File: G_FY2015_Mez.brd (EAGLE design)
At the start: 160 x 100 mm, 205 parts, among them IC100 FT232RL, IC101 FT245RL, J100 EPL.00.250.NTN, J101 IL-2P-S3EN2, J110 EPL.00.250.NTN, J111 IL-2P-S3EN2, J120 EPL.00.250.NTN, J121 IL-2P-S3EN2, J130 EPL.00.250.NTN, J131 IL-2P-S3EN2, J180 TOKUDEN_SP6, J181 USB Mini-B Connector, J182 USB Mini-B Connector, J300 SHV_PIGTAIL_LAND, J301 SHV_PIGTAIL_LAND, J400 RPI2_GPIO_HOLES, J410 IL-3P-S3EN2, J411 IL-3P-S3EN2, J600_12V IL-4P-S3EN2, J610 2.1MMJACKTHM, J620 IL-2P-S3EN2, J630 USB_TYPEA_LUMBERG_2410_01, J640 USB_TYPEA_LUMBERG_2410_01, J650_VOUT IL-4P-S3EN2, U100 AD9215LONG_PAD, U101 AD8138, U102 LM6172, U110 AD9215LONG_PAD, U111 AD8138, U112 LM6172, U120 AD9215LONG_PAD, U121 AD8138, U130 AD9215LONG_PAD, U131 AD8138, U191 GPS_FGPMMOPA6H, U300 OPTON_1PA_12, U301 OPTON_1PA_12, U302 2SC1815, U303 2SJ681, U410 MCP3208-CI/SL, U411 MCP1525TSOT-23-3, U412 LM60, U413 LM60, U500 LT6106, U510 LT6106, U520 2SC1815, U521 2SJ681, U600 PHT12050WAH, U610 PHT12050WAH, U620 LTC1983ES6-3, U621 LTC1983ES6-5

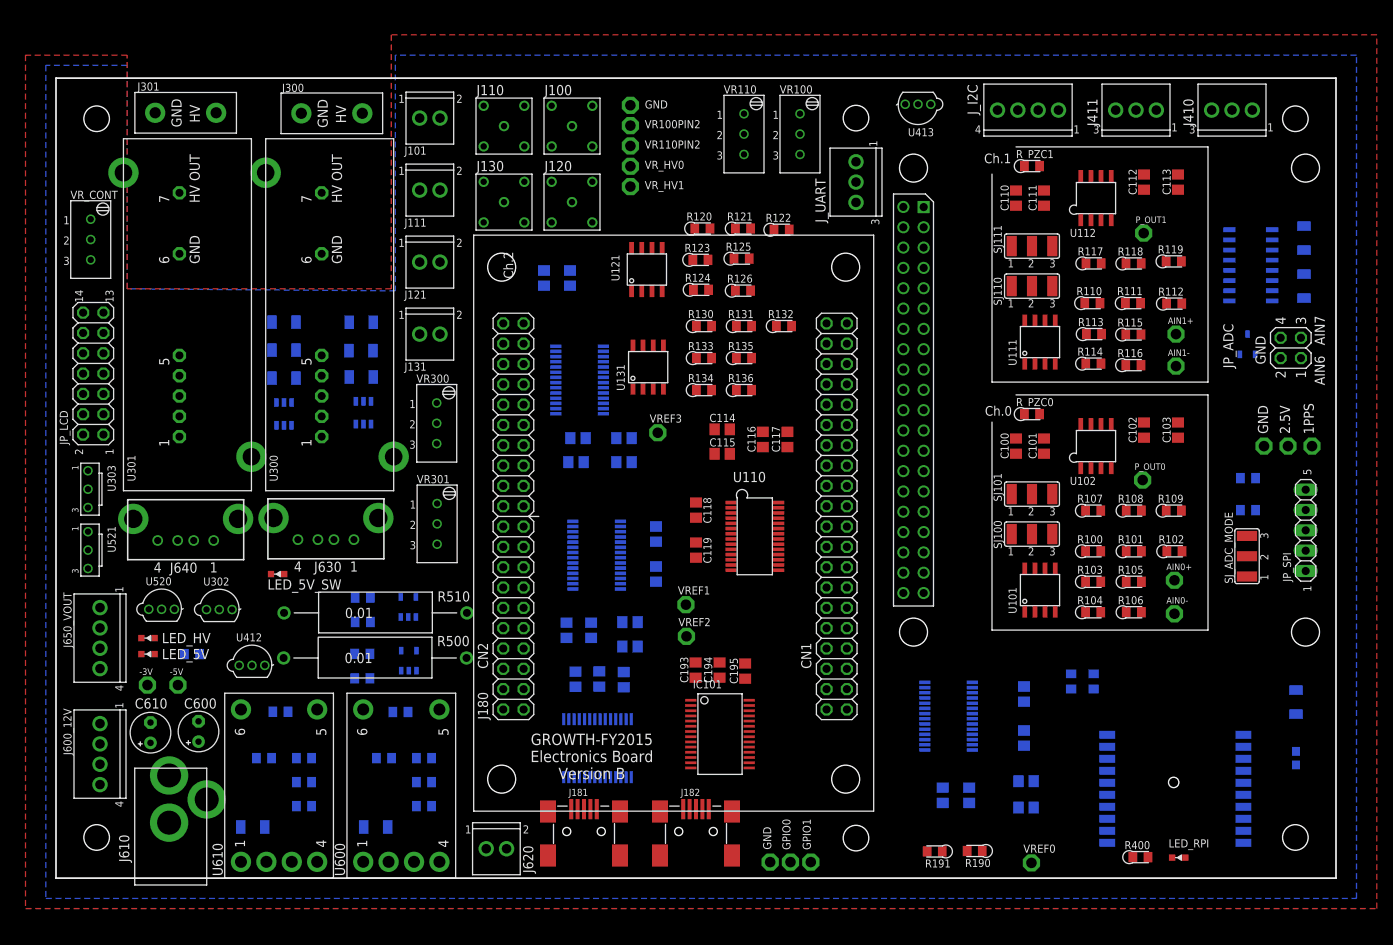
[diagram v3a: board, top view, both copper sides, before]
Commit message: Ch.0 and Ch.1 connector modified, slow ADC and Ras Pi locations modified
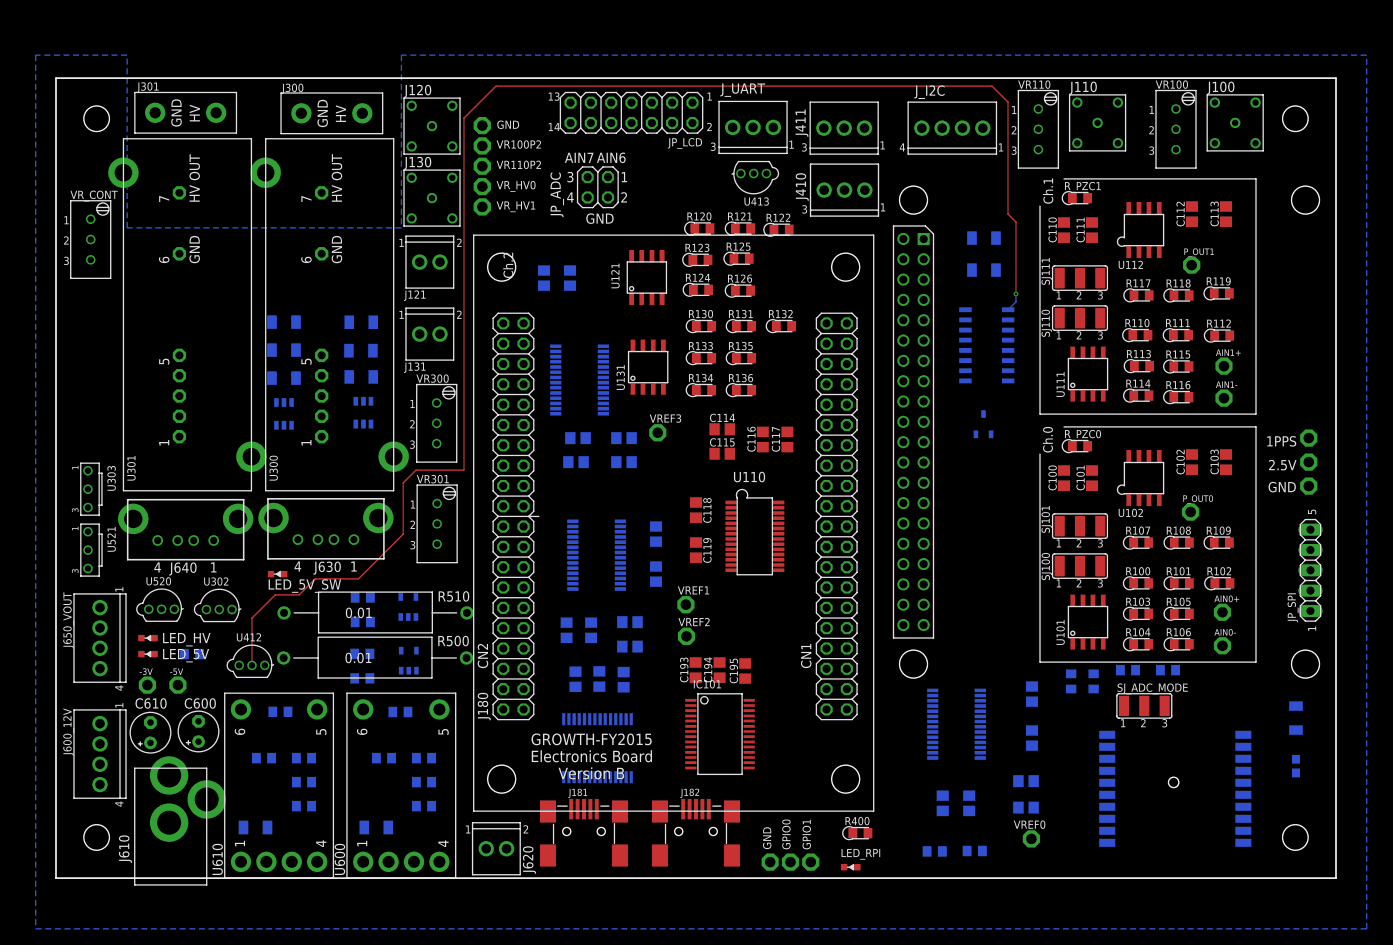
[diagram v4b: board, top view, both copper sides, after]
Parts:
- removed J101, J111: IL-2P-S3EN2, Aardvark:IL-2P-S3EN2
- removed VR100PIN2, VR110PIN2: TPPAD1-13, Aardvark:P1-13
- added VR100P2, VR110P2: TPPAD1-13, Aardvark:P1-13
- moved JP_ADC 88.9 mm to (67.7, 86.3), turned to 180 degrees
- moved J100 82.9 mm to (147.4, 94.4)
- moved JP_LCD 74.8 mm to (71.9, 95.7), turned to 180 degrees
- moved J110 74.2 mm to (130.2, 94.4)
- moved J410 49.5 mm to (98.6, 86.0)
- moved VR100 47.0 mm to (140.0, 93.6)
- moved LED_RPI 41.0 mm to (99.3, 1.36)
- moved C411 40.0 mm to (116.0, 76.0), turned to 0 degrees
- moved C410 40.0 mm to (116.0, 80.0), turned to 0 degrees
- moved VR110 36.8 mm to (122.8, 93.6)
- moved J411 36.5 mm to (98.5, 93.7)
- moved R400 35.1 mm to (100.6, 5.62)
- moved U410 34.5 mm to (116.3, 66.6)
- moved U411 34.5 mm to (115.9, 56.7)
- moved R192 26.0 mm to (139.0, 26.0)
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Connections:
- net AIN_0: no longer J101.P$1
- net AIN_1: no longer J111.P$1
- net GND: no longer J101.P$2, J111.P$2
- net N$62: now also VR110P2.TP; no longer VR110PIN2.TP
- net N$73: now also VR100P2.TP; no longer VR100PIN2.TP
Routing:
- net SLOWADC_0: track 0.00 -> 185.1 mm, vias 0 -> 1
- removed copper zone on layer 1, net GND

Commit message: VR_CONT location modified
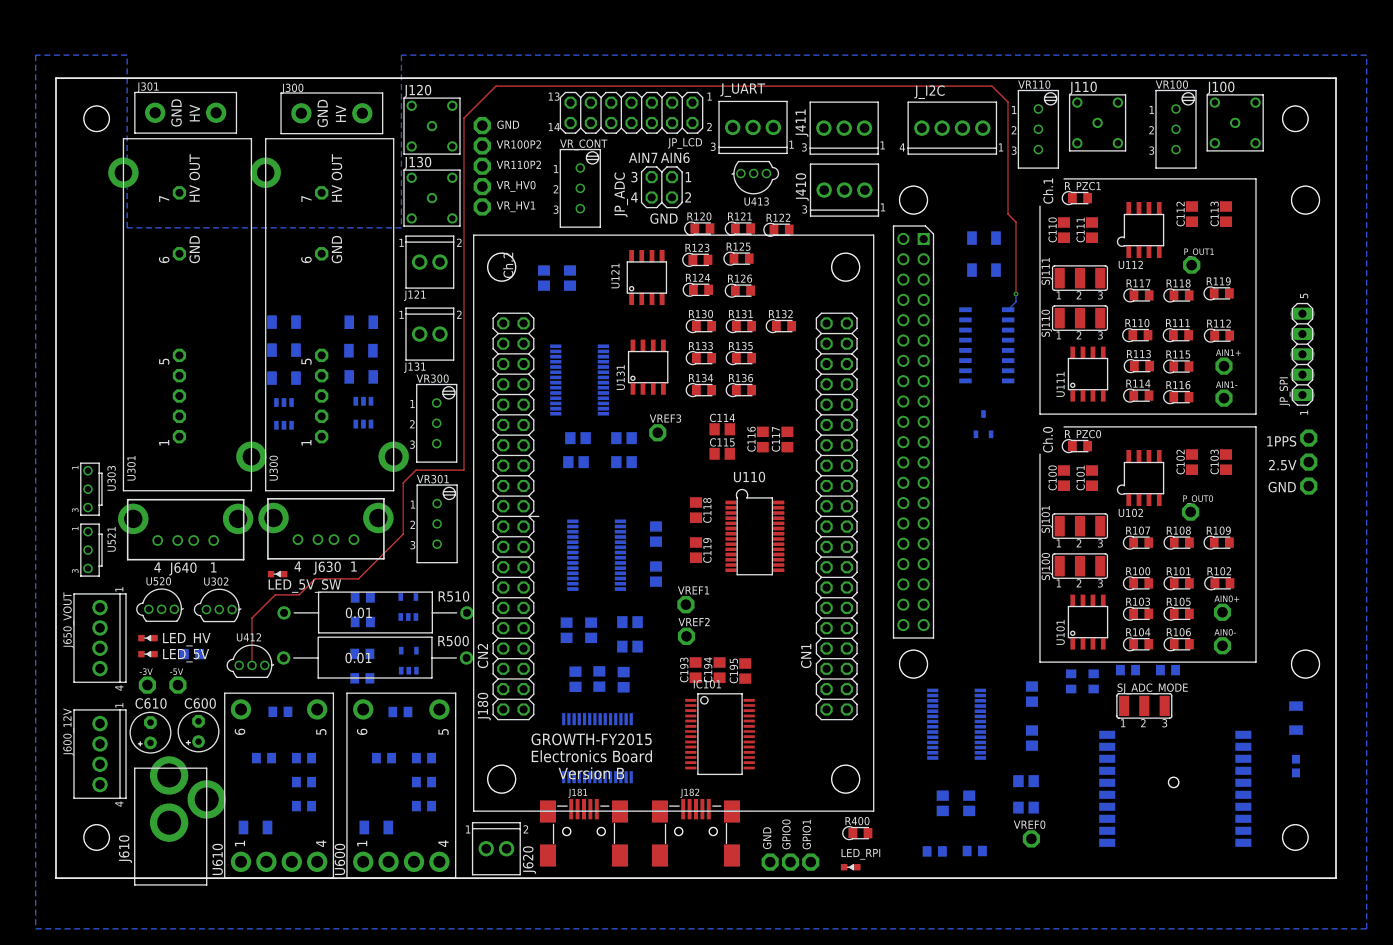
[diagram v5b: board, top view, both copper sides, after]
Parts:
- moved VR_CONT 61.5 mm to (65.5, 86.2)
- moved JP_SPI 27.0 mm to (155.8, 65.5)
- moved JP_ADC 8.00 mm to (75.7, 86.3)
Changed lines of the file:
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@@
 <layer number="17" name="Pads" color="2" fill="1" visible="yes" active="yes"/>
 <layer number="18" name="Vias" color="2" fill="1" visible="yes" active="yes"/>
-<layer number="19" name="Unrouted" color="6" fill="1" visible="yes" active="yes"/>
+<layer number="19" name="Unrouted" color="6" fill="1" visible="no" active="yes"/>
 <layer number="20" name="Dimension" color="15" fill="1" visible="yes" active="yes"/>
 <layer number="21" name="tPlace" color="7" fill="1" visible="yes" active="yes"/>
@@
 <wire x1="150" y1="87.4" x2="126" y2="87.4" width="0.127" layer="21"/>
 <text x="89.408" y="3.556" size="1.016" layer="21" rot="R90">GND</text>
-<text x="66.2" y="81.8" size="1.27" layer="21">GND</text>
-<text x="67.6" y="89.4" size="1.27" layer="21">AIN6</text>
-<text x="63.6" y="89.4" size="1.27" layer="21">AIN7</text>
+<text x="74.2" y="81.8" size="1.27" layer="21">GND</text>
+<text x="75.6" y="89.4" size="1.27" layer="21">AIN6</text>
+<text x="71.6" y="89.4" size="1.27" layer="21">AIN7</text>
 <text x="55.09" y="93.66" size="1.016" layer="21">GND</text>
 </plain>
@@
 <attribute name="OC_FARNELL" value="3817866" x="116.85" y="-52.16" size="1.778" layer="27" display="off"/>
 </element>
-<element name="JP_ADC" library="Aardvark" package="2X02" value="" x="67.73" y="86.35" smashed="yes" rot="R180">
-<attribute name="NAME" x="61.825" y="88.27" size="1.27" layer="25" ratio="10" rot="R270"/>
-<attribute name="VALUE" x="70.27" y="90.795" size="1.27" layer="27" rot="R180"/>
+<element name="JP_ADC" library="Aardvark" package="2X02" value="" x="75.73" y="86.35" smashed="yes" rot="R180">
+<attribute name="NAME" x="69.825" y="88.27" size="1.27" layer="25" ratio="10" rot="R270"/>
+<attribute name="VALUE" x="78.27" y="90.795" size="1.27" layer="27" rot="R180"/>
 </element>
 <element name="R510" library="Aardvark" package="R_LVR03" value="0.01" x="39.934" y="33.152" smashed="yes">
@@
 </element>
 <element name="JP_LCD" library="Aardvark" package="LCD16X2" value="LCD16X2" x="71.94" y="95.66" rot="R180"/>
-<element name="VR_CONT" library="Aardvark" package="ADJRP3-9.70XW5.0X9.80MM" value="5k" x="4.34" y="79.82">
-<attribute name="MPN" value="T93YA103KT20" x="4.34" y="79.82" size="1.778" layer="27" display="off"/>
+<element name="VR_CONT" library="Aardvark" package="ADJRP3-9.70XW5.0X9.80MM" value="5k" x="65.54" y="86.22">
+<attribute name="MPN" value="T93YA103KT20" x="65.54" y="86.22" size="1.778" layer="27" display="off"/>
 </element>
 <element name="J650_VOUT" library="Aardvark" package="IL-4P-S3EN2" value="IL-4P-S3EN2" x="5.5" y="30" rot="R270"/>
@@
 <attribute name="VALUE" x="127.8999" y="70" size="0.02" layer="27"/>
 </element>
-<element name="JP_SPI" library="Aardvark" package="1X05" value="" x="156.81" y="38.47" rot="R90"/>
+<element name="JP_SPI" library="Aardvark" package="1X05" value="" x="155.81" y="65.47" rot="R90"/>
 <element name="LED_HV" library="Aardvark" package="LED_1608" value="SML-311WTT86" x="11.5" y="30" smashed="yes" rot="R270">
 <attribute name="NAME" x="13.23" y="29.37" size="1.27" layer="21"/>
@@
 <contactref element="U410" pad="12"/>
 <contactref element="JP_SPI" pad="2"/>
-<wire x1="156.81" y1="35.93" x2="113.68" y2="65.965" width="0" layer="19" extent="16-16"/>
+<wire x1="155.81" y1="62.93" x2="113.68" y2="65.965" width="0" layer="19" extent="16-16"/>
 <wire x1="108.4582" y1="54.4934" x2="113.68" y2="65.965" width="0" layer="19" extent="16-16"/>
 </signal>
@@
 <contactref element="U410" pad="13"/>
 <contactref element="JP_SPI" pad="1"/>
-<wire x1="156.81" y1="33.39" x2="113.68" y2="67.235" width="0" layer="19" extent="16-16"/>
+<wire x1="155.81" y1="60.39" x2="113.68" y2="67.235" width="0" layer="19" extent="16-16"/>
 <wire x1="108.4582" y1="51.9534" x2="113.68" y2="67.235" width="0" layer="19" extent="16-16"/>
 </signal>
@@
 <contactref element="U410" pad="10"/>
 <contactref element="JP_SPI" pad="4"/>
-<wire x1="156.81" y1="41.01" x2="113.68" y2="63.425" width="0" layer="19" extent="16-16"/>
+<wire x1="155.81" y1="68.01" x2="113.68" y2="63.425" width="0" layer="19" extent="16-16"/>
 <wire x1="105.9182" y1="51.9534" x2="113.68" y2="63.425" width="0" layer="19" extent="16-16"/>
 </signal>
@@
 <contactref element="J400" pad="P$26"/>
 <contactref element="JP_SPI" pad="5"/>
-<wire x1="105.9182" y1="49.4134" x2="156.81" y2="43.55" width="0" layer="19" extent="1-1"/>
+<wire x1="105.9182" y1="49.4134" x2="155.81" y2="70.55" width="0" layer="19" extent="1-1"/>
 </signal>
 <signal name="SPI_MOSI">
@@
 <contactref element="U410" pad="11"/>
 <contactref element="JP_SPI" pad="3"/>
-<wire x1="156.81" y1="38.47" x2="113.68" y2="64.695" width="0" layer="19" extent="16-16"/>
+<wire x1="155.81" y1="65.47" x2="113.68" y2="64.695" width="0" layer="19" extent="16-16"/>
 <wire x1="108.4582" y1="57.0334" x2="113.68" y2="64.695" width="0" layer="19" extent="16-16"/>
 </signal>
@@
 <contactref element="U410" pad="7"/>
 <contactref element="JP_ADC" pad="1"/>
-<wire x1="69" y1="87.62" x2="119.02" y2="63.425" width="0" layer="19" extent="16-16"/>
+<wire x1="77" y1="87.62" x2="119.02" y2="63.425" width="0" layer="19" extent="16-16"/>
 </signal>
 <signal name="SLOWADC_7">
 <contactref element="U410" pad="8"/>
 <contactref element="JP_ADC" pad="3"/>
-<wire x1="66.46" y1="87.62" x2="119.02" y2="62.155" width="0" layer="19" extent="16-16"/>
+<wire x1="74.46" y1="87.62" x2="119.02" y2="62.155" width="0" layer="19" extent="16-16"/>
 </signal>
 <signal name="VREF_2V5">
@@
 <wire x1="117.5" y1="80" x2="85.61" y2="88.072" width="0" layer="19" extent="16-16"/>
 <wire x1="117.5" y1="76" x2="117.5" y2="80" width="0" layer="19" extent="16-16"/>
-<wire x1="66.46" y1="85.08" x2="117.5" y2="76" width="0" layer="19" extent="16-16"/>
-<wire x1="69" y1="85.08" x2="66.46" y2="85.08" width="0" layer="19" extent="1-1"/>
-<wire x1="115.94" y1="58.01" x2="66.46" y2="85.08" width="0" layer="19" extent="16-16"/>
+<wire x1="74.46" y1="85.08" x2="117.5" y2="76" width="0" layer="19" extent="16-16"/>
+<wire x1="77" y1="85.08" x2="74.46" y2="85.08" width="0" layer="19" extent="1-1"/>
+<wire x1="115.94" y1="58.01" x2="74.46" y2="85.08" width="0" layer="19" extent="16-16"/>
 <wire x1="113.68" y1="62.155" x2="115.94" y2="58.01" width="0" layer="19" extent="16-16"/>
 <wire x1="113.68" y1="68.505" x2="113.68" y2="62.155" width="0" layer="19" extent="16-16"/>
@@
 <wire x1="139.68" y1="67.87" x2="141.65" y2="72.83" width="0" layer="19" extent="1-1"/>
 <wire x1="134.6" y1="67.87" x2="139.68" y2="67.87" width="0" layer="19" extent="1-1"/>
-<wire x1="156.6" y1="49" x2="69" y2="85.08" width="0" layer="19" extent="1-1"/>
+<wire x1="156.6" y1="49" x2="77" y2="85.08" width="0" layer="19" extent="1-1"/>
 <wire x1="133.05" y1="26" x2="156.6" y2="49" width="0" layer="19" extent="16-16"/>
 <wire x1="133.5" y1="21.52" x2="133.05" y2="26" width="0" layer="19" extent="1-16"/>
@@
 <wire x1="39.298" y1="32.01" x2="44.038" y2="32.63" width="0" layer="19" extent="16-16"/>
 <wire x1="15.43" y1="78.04" x2="26.21" y2="88.17" width="0" layer="19" extent="1-1"/>
-<wire x1="4.34" y1="77.28" x2="15.43" y2="78.04" width="0" layer="19" extent="1-1"/>
-<wire x1="8.43" y1="88.17" x2="4.34" y2="77.28" width="0" layer="19" extent="1-1"/>
+<wire x1="65.54" y1="83.68" x2="15.43" y2="78.04" width="0" layer="19" extent="1-1"/>
+<wire x1="8.43" y1="88.17" x2="65.54" y2="83.68" width="0" layer="19" extent="1-1"/>
 <wire x1="12.398" y1="95.664" x2="8.43" y2="88.17" width="0" layer="19" extent="1-1"/>
 <wire x1="148.418" y1="7.41" x2="98.515" y2="1.36" width="0" layer="19" extent="1-16"/>
@@
 <wire x1="36.65" y1="69.49" x2="39.38" y2="59.6" width="0" layer="19" extent="16-16"/>
 <wire x1="27" y1="69.5" x2="36.65" y2="69.49" width="0" layer="19" extent="16-16"/>
-<wire x1="4.34" y1="82.36" x2="27" y2="69.5" width="0" layer="19" extent="16-16"/>
+<wire x1="65.54" y1="88.76" x2="27" y2="69.5" width="0" layer="19" extent="16-16"/>
 </signal>
 <signal name="N$56">
@@
 <contactref element="JP_LCD" pad="3"/>
 <contactref element="VR_CONT" pad="2"/>
-<wire x1="77.02" y1="96.93" x2="4.34" y2="79.82" width="0" layer="19" extent="1-1"/>
+<wire x1="77.02" y1="96.93" x2="65.54" y2="86.22" width="0" layer="19" extent="1-1"/>
 </signal>
 <signal name="LCD_RS">

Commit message: LM60 (near DCDC) moved. Hand wiring necessary while integration
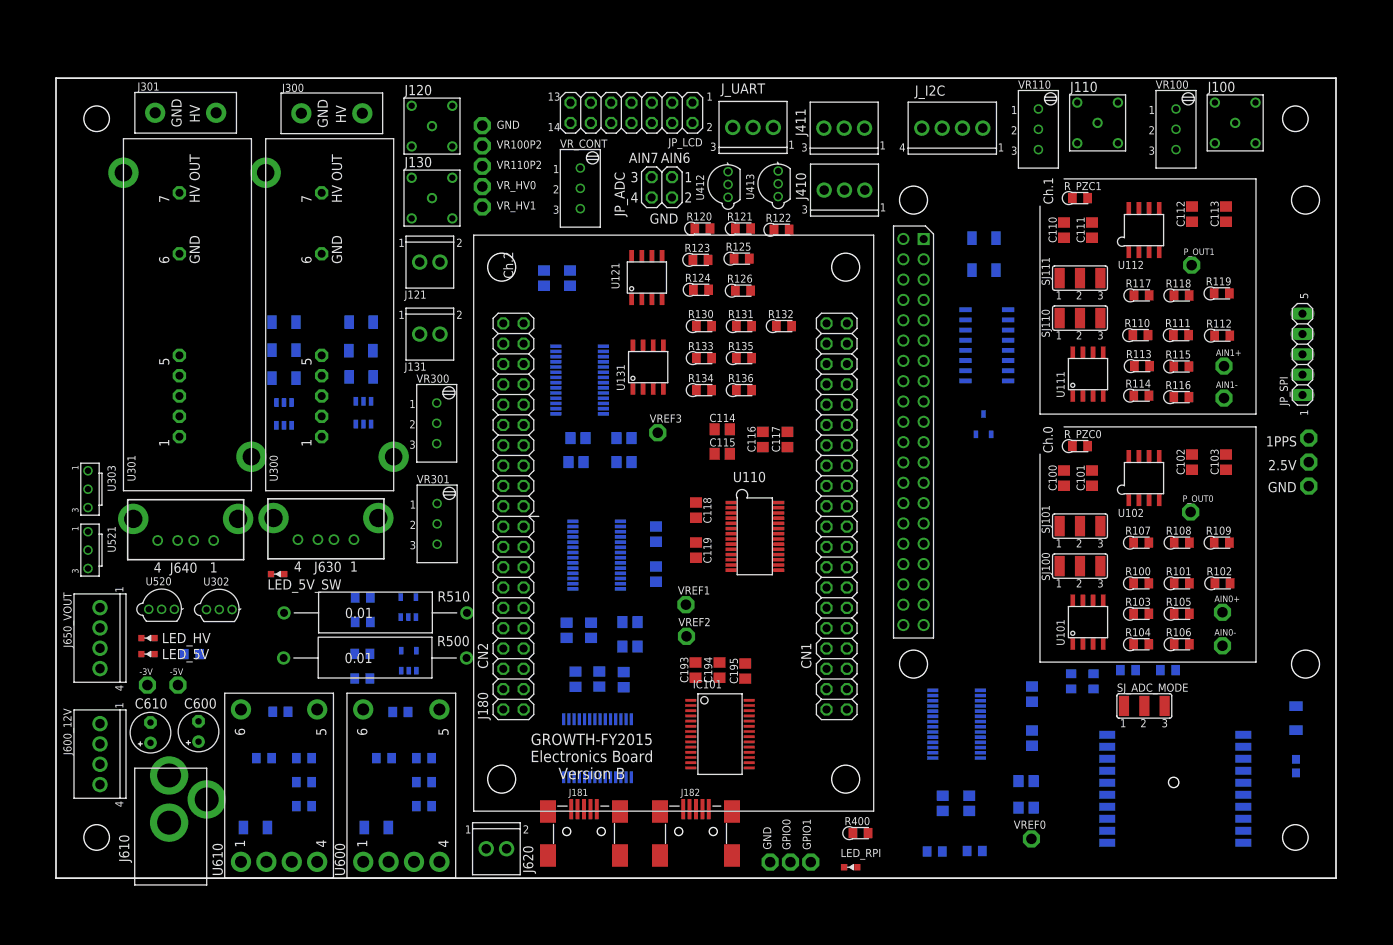
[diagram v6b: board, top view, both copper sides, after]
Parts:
- moved U412 84.6 mm to (84.0, 86.7), turned to 90 degrees
- moved U413 3.32 mm to (90.3, 86.8), turned to 90 degrees
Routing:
- net SLOWADC_0: track 185.1 -> 0.00 mm, vias 1 -> 0
- removed copper zone on layer 16, net GND

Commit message: P板.comに注文した時のバージョン
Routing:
- net GND: track 0.00 -> 1308.8 mm, vias 0 -> 27
- net +3V3: track 0.00 -> 487.4 mm, vias 0 -> 22
- net +5V: track 0.00 -> 432.9 mm, vias 0 -> 11
- net -5V: track 0.00 -> 238.8 mm, vias 0 -> 8
- net -3V3: track 0.00 -> 220.1 mm, vias 0 -> 6
- net ADC_CM: track 0.00 -> 143.1 mm, vias 0 -> 3
- net GPS_1PPS: track 0.00 -> 133.3 mm, vias 0 -> 2
- net N$73: track 0.00 -> 130.4 mm, vias 0 -> 1
- net SLOWADC_4: track 0.00 -> 125.6 mm, vias 0 -> 3
- net ADC_MODE: track 0.00 -> 110.4 mm, vias 0 -> 6
- net +12V: track 0.00 -> 109.5 mm, vias 0 -> 1
- net SLOWADC_5: track 0.00 -> 108.1 mm, vias 0 -> 6
- net LCD_D7: track 0.00 -> 100.5 mm, vias 0 -> 3
- net LCD_D4: track 0.00 -> 99.8 mm, vias 0 -> 3
- net LCD_D6: track 0.00 -> 96.2 mm, vias 0 -> 2
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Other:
- board text removed: "Ch.2"
